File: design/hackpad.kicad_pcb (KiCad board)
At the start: 2 copper layers, 70.9 x 88 mm, 38 parts, among them SW1 SW_Push, SW10 RotaryEncoder, SW2 SW_Push, SW3 SW_Push, SW4 SW_Push, SW5 SW_Push, SW6 SW_Push, SW7 SW_Push, SW8 SW_Push, SW9 SW_Push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

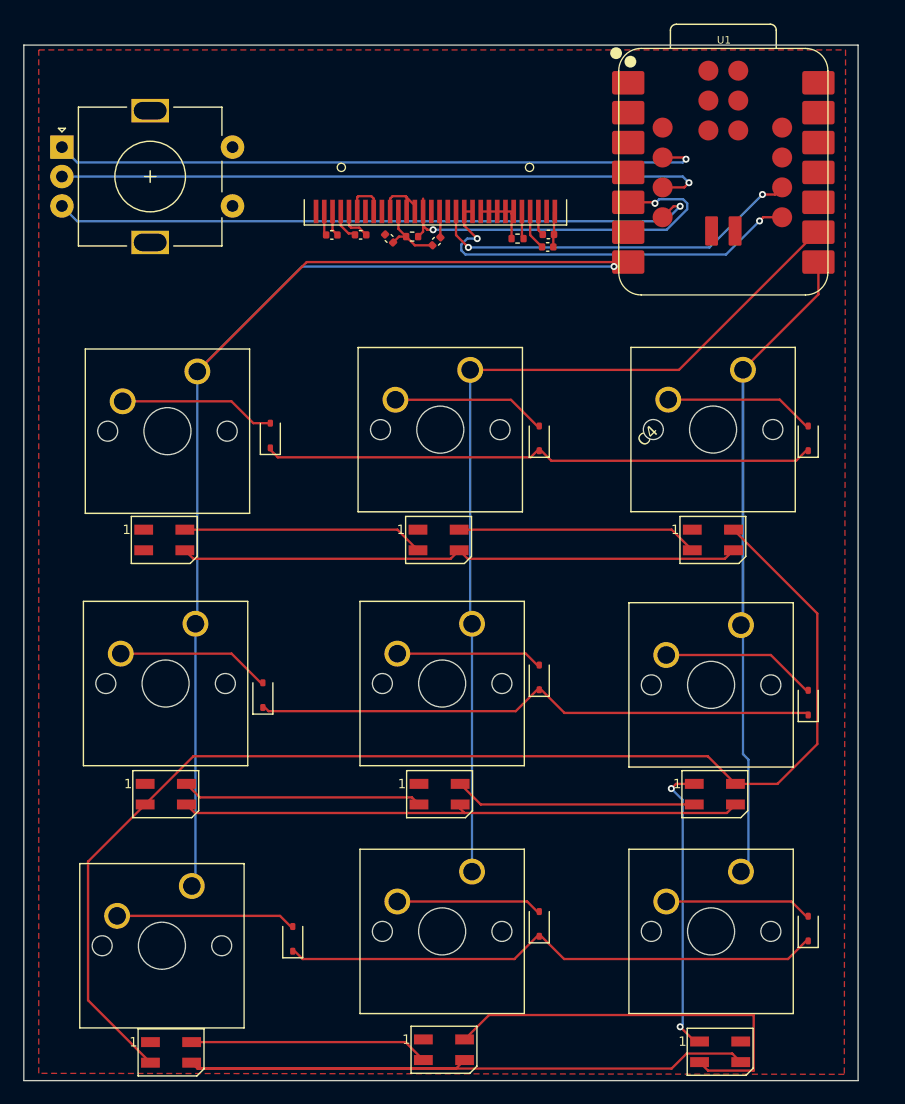
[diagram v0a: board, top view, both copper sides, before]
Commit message: add firmware, forgor to add the 5v net
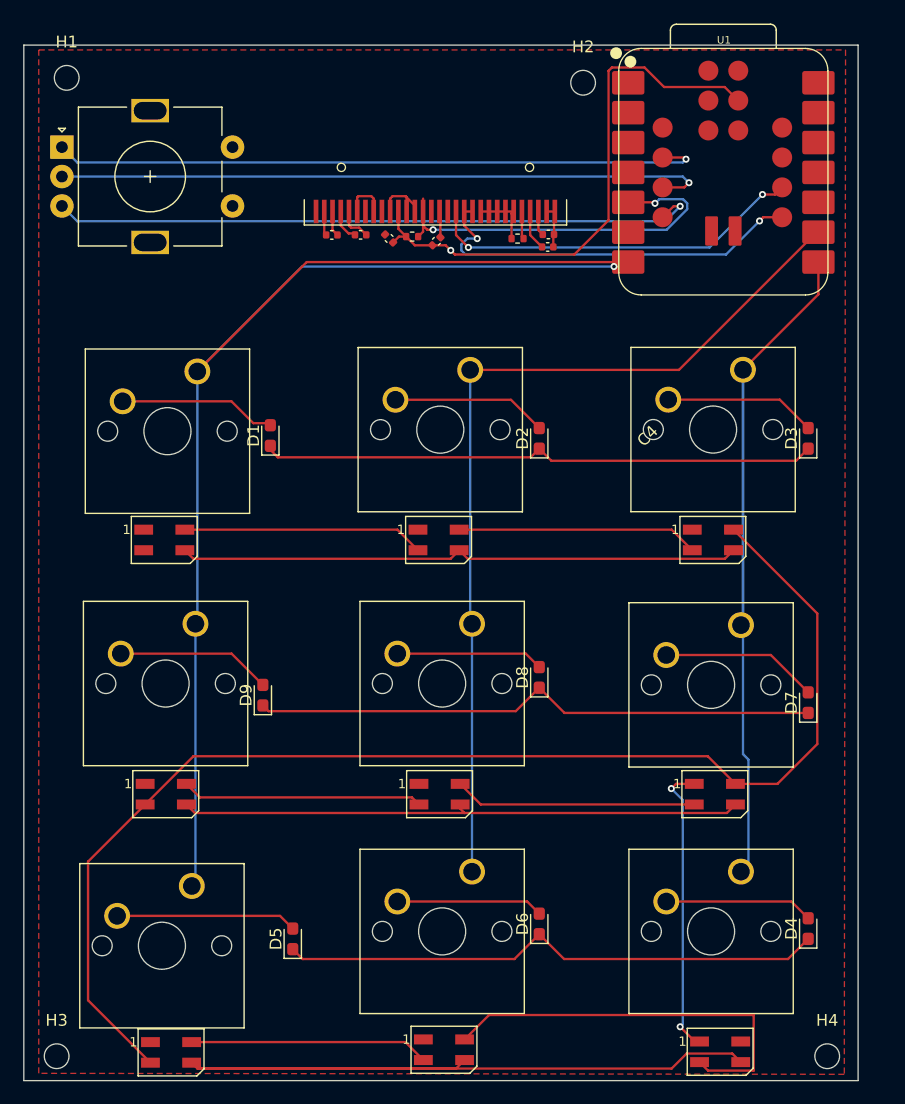
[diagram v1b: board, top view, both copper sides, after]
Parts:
- added H1: MountingHole, MountingHole:MountingHole_2.1mm, F.Cu at (223.4, 31.6)
- added H2: MountingHole, MountingHole:MountingHole_2.1mm, F.Cu at (267.2, 32.0)
- added H3: MountingHole, MountingHole:MountingHole_2.1mm, F.Cu at (222.5, 114.8)
- added H4: MountingHole, MountingHole:MountingHole_2.1mm, F.Cu at (288.0, 114.8)
- D1, D2, D3, D4, D5, D6, D7, D8, D9: footprint Diode_SMD:D_SOD-323 -> Diode_SMD:D_0603_1608Metric_Pad1.05x0.95mm_HandSolder
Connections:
- U1 pad 14: unconnected-(U1-VBUS-Pad14) -> 5V
- U1 pad 26: unconnected-(U1-3V3_1-Pad26) -> +3V3
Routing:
- net +3V3: track 6.26 -> 47.8 mm, vias 0 -> 1
- net GND: track 44.0 -> 44.7 mm

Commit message: updatre hackpad,  add assemblie(s)
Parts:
- moved SW10 2.29 mm to (223.2, 39.8)
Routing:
- net Net-(U1-GPIO12_D16_SPI1_MISO): track 55.9 -> 58.7 mm
- net Net-(U1-GPIO10_D17_SPI1_SCK): track 55.8 -> 57.8 mm
- net Net-(U1-GPIO11_D15_SPI1_MOSI): track 55.5 -> 57.5 mm
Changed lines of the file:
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@@
 	(footprint "Rotary_Encoder:RotaryEncoder_Alps_EC11E-Switch_Vertical_H20mm"
 		(layer "F.Cu")
-		(at 222.95 37.475)
+		(at 223.25 39.75)
 		(descr "Alps rotary encoder, EC11E... with switch, vertical shaft, http://www.alps.com/prod/info/E/HTML/Encoder/Incremental/EC11/EC11E15204A3.html")
 		(tags "rotary encoder")
@@
 		)
 		(embedded_fonts no)
-		(model "${KICAD10_3DMODEL_DIR}/Button_Switch_Keyboard.3dshapes/SW_Cherry_MX_1.00u_PCB.step"
+		(model "/home/ttf/Downloads/cherry-mx-switch-5.snapshot.2/MX .STEP"
 			(offset
 				(xyz 0 0 0)
@@
 		)
 		(embedded_fonts no)
-		(model "${KICAD10_3DMODEL_DIR}/Button_Switch_Keyboard.3dshapes/SW_Cherry_MX_1.00u_PCB.step"
+		(model "/home/ttf/Downloads/cherry-mx-switch-5.snapshot.2/MX .STEP"
 			(offset
 				(xyz 0 0 0)
@@
 	)
 	(segment
+		(start 274.75 38.5)
+		(end 276 38.5)
+		(width 0.2)
+		(layer "B.Cu")
+		(net "Net-(U1-GPIO10_D17_SPI1_SCK)")
+	)
+	(segment
 		(start 222.95 37.475)
 		(end 224.25 38.775)
@@
 	)
 	(segment
+		(start 274.5 38.75)
+		(end 274.75 38.5)
+		(width 0.2)
+		(layer "B.Cu")
+		(net "Net-(U1-GPIO10_D17_SPI1_SCK)")
+	)
+	(segment
 		(start 275.725 38.775)
 		(end 276 38.5)
@@
 	)
 	(segment
-		(start 224.25 38.775)
-		(end 275.725 38.775)
+		(start 274.2 38.45)
+		(end 274.5 38.75)
+		(width 0.2)
+		(layer "B.Cu")
+		(net "Net-(U1-GPIO10_D17_SPI1_SCK)")
+	)
+	(segment
+		(start 224.55 38.45)
+		(end 274.2 38.45)
+		(width 0.2)
+		(layer "B.Cu")
+		(net "Net-(U1-GPIO10_D17_SPI1_SCK)")
+	)
+	(segment
+		(start 223.25 39.75)
+		(end 224.55 38.45)
 		(width 0.2)
 		(layer "B.Cu")
@@
 	)
 	(segment
-		(start 224.25 43.775)
-		(end 274.225 43.775)
+		(start 255.651471 42.5)
+		(end 257.251471 44.1)
 		(width 0.2)
 		(layer "B.Cu")
@@
 	)
 	(segment
-		(start 274.225 43.775)
+		(start 273.9 44.1)
 		(end 275.5 42.5)
 		(width 0.2)
@@
 	)
 	(segment
-		(start 222.95 42.475)
-		(end 224.25 43.775)
+		(start 223.25 44.75)
+		(end 224.55 46.05)
+		(width 0.2)
+		(layer "B.Cu")
+		(net "Net-(U1-GPIO11_D15_SPI1_MOSI)")
+	)
+	(segment
+		(start 224.55 46.05)
+		(end 252.101471 46.05)
+		(width 0.2)
+		(layer "B.Cu")
+		(net "Net-(U1-GPIO11_D15_SPI1_MOSI)")
+	)
+	(segment
+		(start 252.101471 46.05)
+		(end 255.651471 42.5)
+		(width 0.2)
+		(layer "B.Cu")
+		(net "Net-(U1-GPIO11_D15_SPI1_MOSI)")
+	)
+	(segment
+		(start 257.251471 44.1)
+		(end 273.9 44.1)
 		(width 0.2)
 		(layer "B.Cu")
@@
 	)
 	(segment
+		(start 275.5 41.25)
+		(end 276.25 40.5)
+		(width 0.2)
+		(layer "B.Cu")
+		(net "Net-(U1-GPIO12_D16_SPI1_MISO)")
+	)
+	(segment
+		(start 223.25 42.25)
+		(end 224.25 41.25)
+		(width 0.2)
+		(layer "B.Cu")
+		(net "Net-(U1-GPIO12_D16_SPI1_MISO)")
+	)
+	(segment
+		(start 224.25 41.25)
+		(end 275.5 41.25)
+		(width 0.2)
+		(layer "B.Cu")
+		(net "Net-(U1-GPIO12_D16_SPI1_MISO)")
+	)
+	(segment
 		(start 275.725 39.975)
 		(end 276.25 40.5)
@@
 	)
 	(segment
-		(start 222.95 39.975)
-		(end 275.725 39.975)
+		(start 222.95 42.475)
+		(end 224.25 43.775)
 		(width 0.2)
 		(layer "B.Cu")

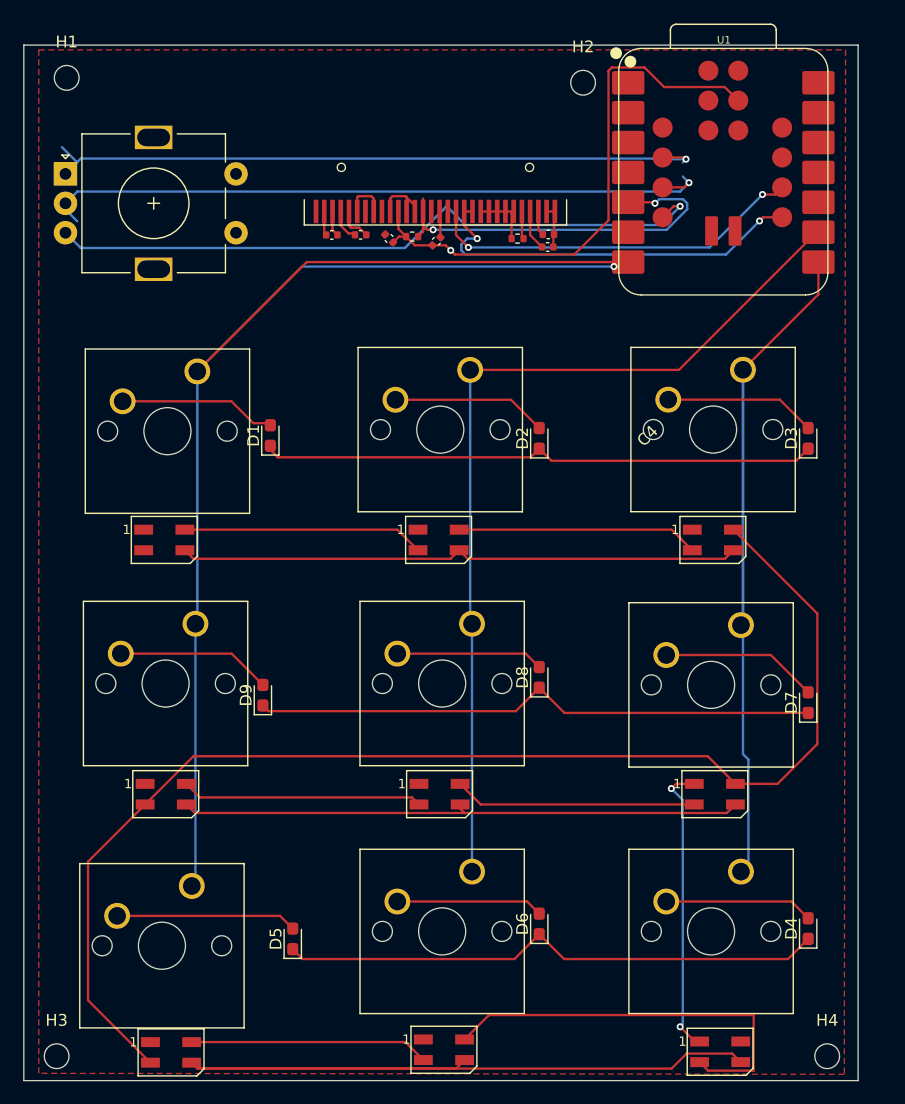
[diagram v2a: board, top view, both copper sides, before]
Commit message: add more silkscreen tezt
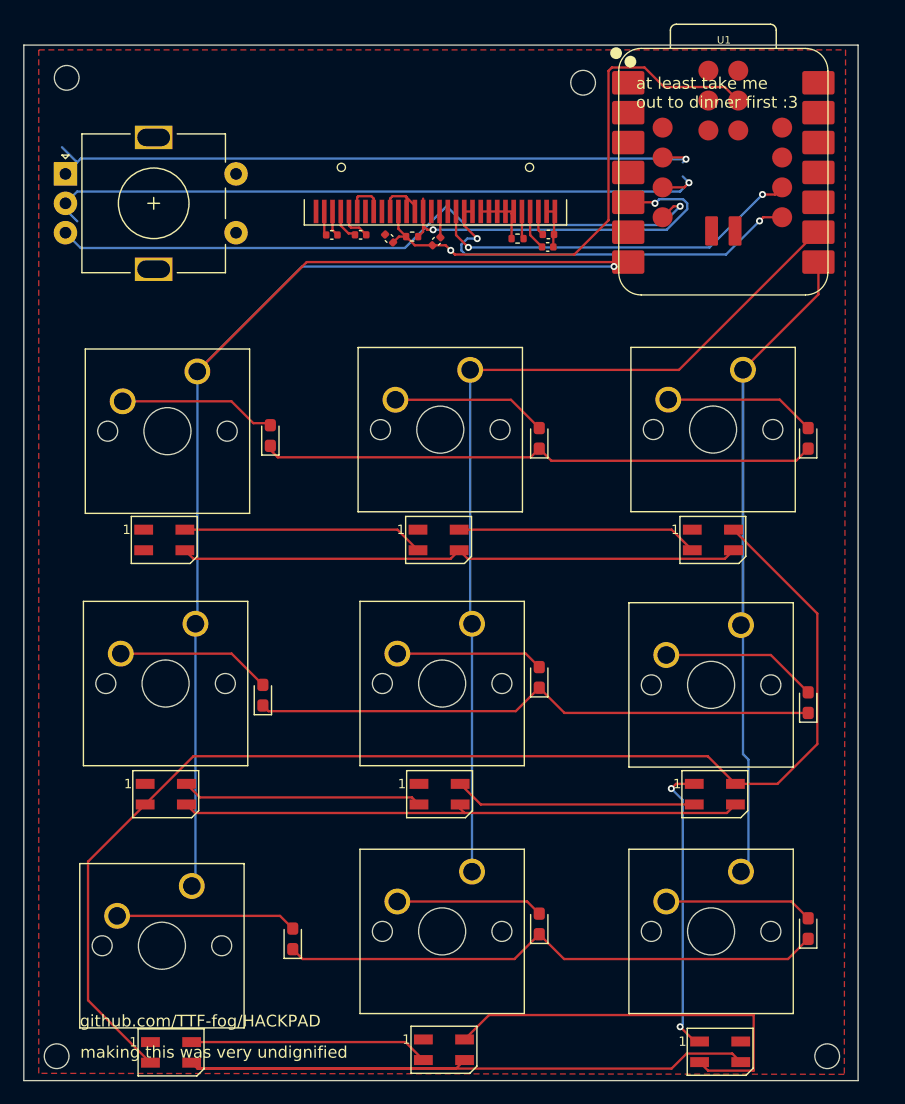
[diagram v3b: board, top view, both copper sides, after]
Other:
- board text added: "at least take me out to dinner first :3"
- board text added: "github.com/TTF-fog/HACKPAD"
- board text added: "making this was very undignified"
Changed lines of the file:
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@@
 			(at 0 -1.43 90)
 			(layer "F.SilkS")
+			(hide yes)
 			(effects
 				(font
@@
 			(at 0 -1.43 90)
 			(layer "F.SilkS")
+			(hide yes)
 			(effects
 				(font
@@
 			(at 0 -1.43 90)
 			(layer "F.SilkS")
+			(hide yes)
 			(effects
 				(font
@@
 			(at 0 -1.43 90)
 			(layer "F.SilkS")
+			(hide yes)
 			(effects
 				(font
@@
 			(at 0 -1.43 90)
 			(layer "F.SilkS")
+			(hide yes)
 			(effects
 				(font
@@
 			(at 0.995 24.39 45)
 			(layer "F.SilkS")
+			(hide yes)
 			(effects
 				(font
@@
 			(at 0 -1.43 90)
 			(layer "F.SilkS")
+			(hide yes)
 			(effects
 				(font
@@
 			(at 0 -1.43 90)
 			(layer "F.SilkS")
+			(hide yes)
 			(effects
 				(font
@@
 			(at 0 -3.05 0)
 			(layer "F.SilkS")
+			(hide yes)
 			(effects
 				(font
@@
 			(at 0 -1.43 90)
 			(layer "F.SilkS")
+			(hide yes)
 			(effects
 				(font
@@
 			(at 0 -3.05 0)
 			(layer "F.SilkS")
+			(hide yes)
 			(effects
 				(font
@@
 			(at 0 -1.43 90)
 			(layer "F.SilkS")
+			(hide yes)
 			(effects
 				(font
@@
 			(at 0 -3.05 0)
 			(layer "F.SilkS")
+			(hide yes)
 			(effects
 				(font
@@
 			(at 0 -3.05 0)
 			(layer "F.SilkS")
+			(hide yes)
 			(effects
 				(font
@@
 		(layer "Edge.Cuts")
 	)
+	(gr_text "github.com/TTF-fog/HACKPAD"
+		(at 224.465 112.345 0)
+		(layer "F.SilkS")
+		(effects
+			(font
+				(size 1 1)
+				(thickness 0.1)
+			)
+			(justify left bottom)
+		)
+	)
+	(gr_text "making this was very undignified"
+		(at 224.5 115 0)
+		(layer "F.SilkS")
+		(effects
+			(font
+				(size 1 1)
+				(thickness 0.1)
+			)
+			(justify left bottom)
+		)
+	)
+	(gr_text "at least take me \nout to dinner first :3"
+		(at 271.75 34.25 0)
+		(layer "F.SilkS")
+		(effects
+			(font
+				(size 1 1)
+				(thickness 0.1)
+			)
+			(justify left bottom)
+		)
+	)
 	(segment
